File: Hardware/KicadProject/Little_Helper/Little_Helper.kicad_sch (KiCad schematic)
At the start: 36 parts, among them J1 USB_B_Micro_Molex_1050171001_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, J2 Conn_01x02_Pin, Q1 DMG3415U, SW1 SW_Push, SW2 SW_Push, SW3 SW_Push, SW4 SW_Push, SW5 SW_Push, SW6 SW_SPST, SW7 SW_Push, SW8 SW_Push, U1 AP2112K-3.3, U2 ESP32-S3-MINI-1, U3 MCP73831-2-OT

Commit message: Change Boot and Reset BTN
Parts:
- SW7, SW8: footprint Button_Switch_SMD:SW_Push_SPST_NO_Alps_SKRK -> Button_Switch_SMD:SW_SPST_CK_RS282G05A3
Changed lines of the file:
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@@
 			)
 		)
-		(property "Footprint" "Button_Switch_SMD:SW_Push_SPST_NO_Alps_SKRK"
+		(property "Footprint" "Button_Switch_SMD:SW_SPST_CK_RS282G05A3"
 			(at 128.27 105.41 0)
 			(effects
@@
 			)
 		)
-		(property "Footprint" "Button_Switch_SMD:SW_Push_SPST_NO_Alps_SKRK"
+		(property "Footprint" "Button_Switch_SMD:SW_SPST_CK_RS282G05A3"
 			(at 160.02 105.41 0)
 			(effects

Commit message: pcb layout v1.0 done
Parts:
- removed D4: BAS16, ba_sot:sot_23, symbol ba_diode:BAS16
- removed J2: Conn_01x02_Pin, Connector_Hirose:Hirose_DF13-02P-1.25DSA_1x02_P1.25mm_Vertical, symbol Connector:Conn_01x02_Pin
- removed Q1: DMG3415U, Package_TO_SOT_SMD:SOT-23, symbol PCM_Transistor_MOSFET_AKL:DMG3415U
- removed R3: R2012_100K, ba_res:r2012, symbol ba_res2012:R2012_100K
- removed SW6: SW_SPST, Button_Switch_SMD:SW_SPDT_CK_JS102011SAQN, symbol Switch:SW_SPST
- removed SW7, SW8: SW_Push, Button_Switch_SMD:SW_SPST_CK_RS282G05A3, symbol Switch:SW_Push
- added D4: BAS16, ba_sot:sot_23, symbol Diode_JLCPCB:BAS16
- added J2, J3: SOLDER_CON_5x2_TOP, ba_connector:solder_con_5x2_top, symbol ba_connector:SOLDER_CON_5x2_TOP
- added MH1: fit_3_1, ba_mechanic:fit_3_1, symbol ba_mechanic:fit_3_1
- added Q1: DMG3415U, Package_TO_SOT_SMD:SOT-23, symbol PCM_Transistor_MOSFET_JLCPCB:DMG3415U
- added R3: 100k, Resistor_SMD:R_0805_2012Metric, symbol Device:R
- added SW6: SW_On_On, Button_Switch_SMD:SW_SPDT_PCM12, symbol Switch_Wolke:SW_On_On
- added SW7, SW8: SW_Tactile_Small, Button_Switch_SMD_JLCPCB:SW_SPST_TS-1088-AR02016, symbol Switch_Wolke:SW_Tactile_Small
- C1, C3, C4, C5, C6, C8: LCSC (none) -> C1713
- D1: footprint Diode_SMD:D_0805_2012Metric -> Diode_SMD:D_SOD-123
- R1: LCSC C115316 -> C17414
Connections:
- net +3.3V: now also D4.1 (A)
- net +BATT: now also Q1.3 (D), SW6.3 (C)
- net BOOT0: now also SW8.2 (A)
- net GND: now also J2.1 (P1), R3.1, SW7.1 (A), SW8.1 (A)
- net NEOPIX_VDD: now also D4.3 (K), Q1.2 (S)
- net RESET: now also SW7.2 (A)
- net VBUS: now also Q1.1 (G), R3.2
- new net: J3.1 (P1), SW6.2 (B)
- no-connect marks 33 -> 34

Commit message: edit pcb and footprints for pcb rev1.1
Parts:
- D3: footprint LED_SMD:LED_WS2812B_PLCC4_5.0x5.0mm_P3.2mm -> led_smd_JLCPCB:LED_WS2812B_JLCPCB_5.0x5.0mm_P3.2mm
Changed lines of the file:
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@@
 			)
 		)
-		(property "Footprint" "LED_SMD:LED_WS2812B_PLCC4_5.0x5.0mm_P3.2mm"
+		(property "Footprint" "led_smd_JLCPCB:LED_WS2812B_JLCPCB_5.0x5.0mm_P3.2mm"
 			(at 207.01 129.54 0)
 			(effects

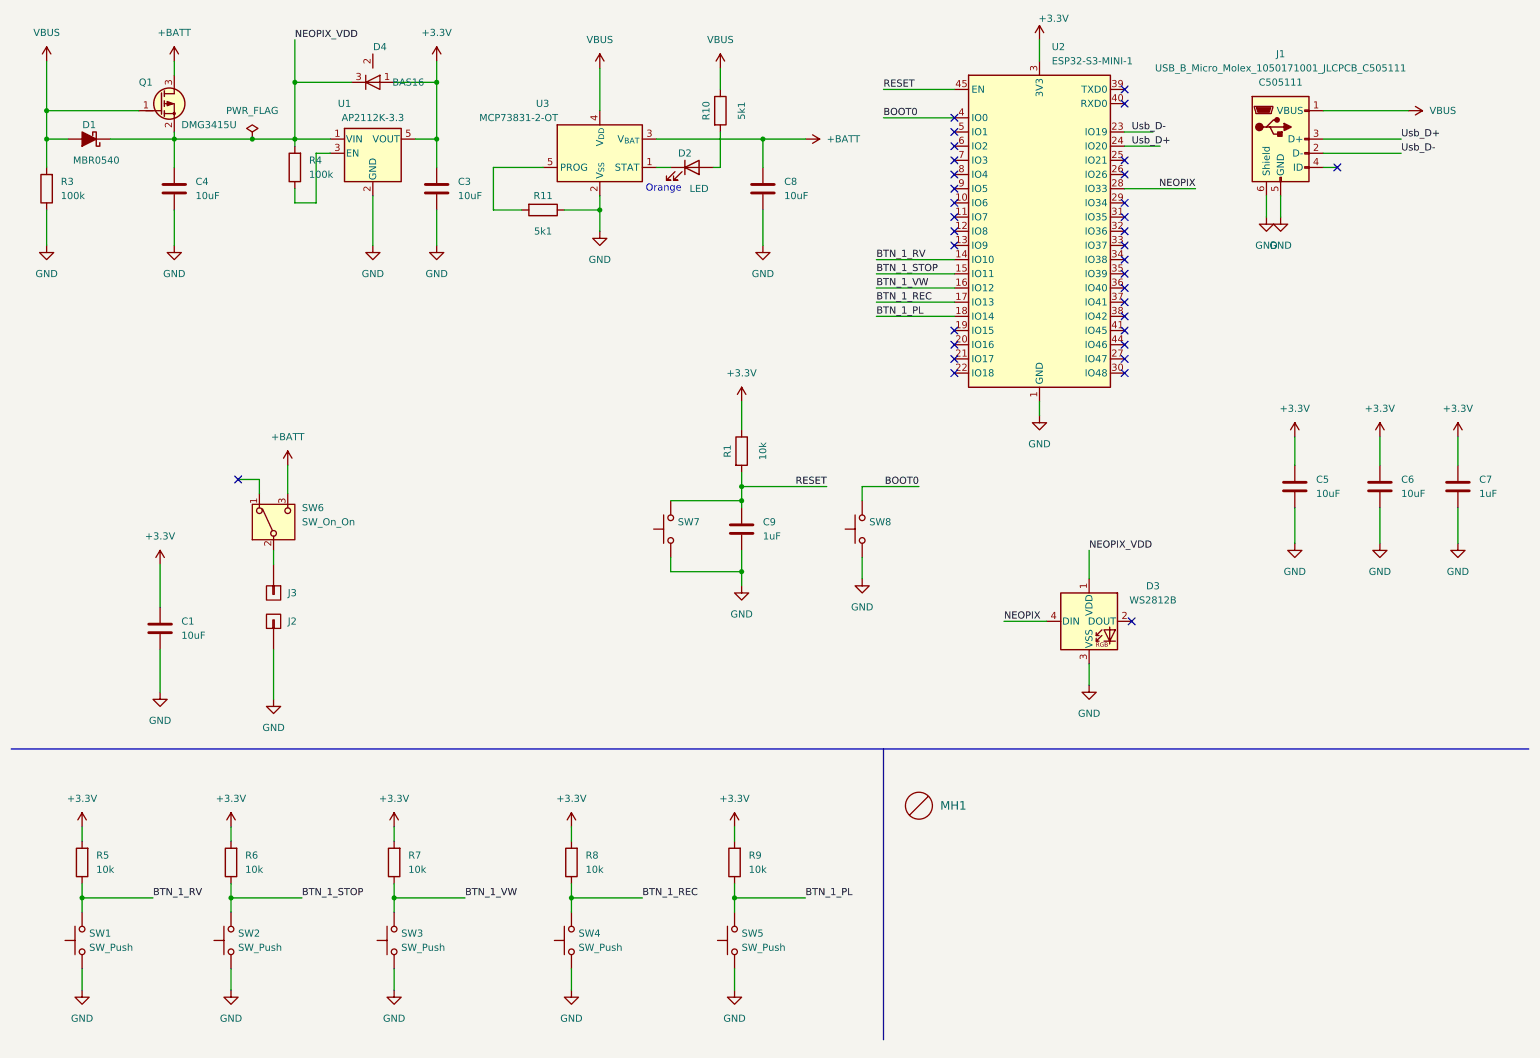
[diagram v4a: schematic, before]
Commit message: pcb v1.1 add second ws2812 led
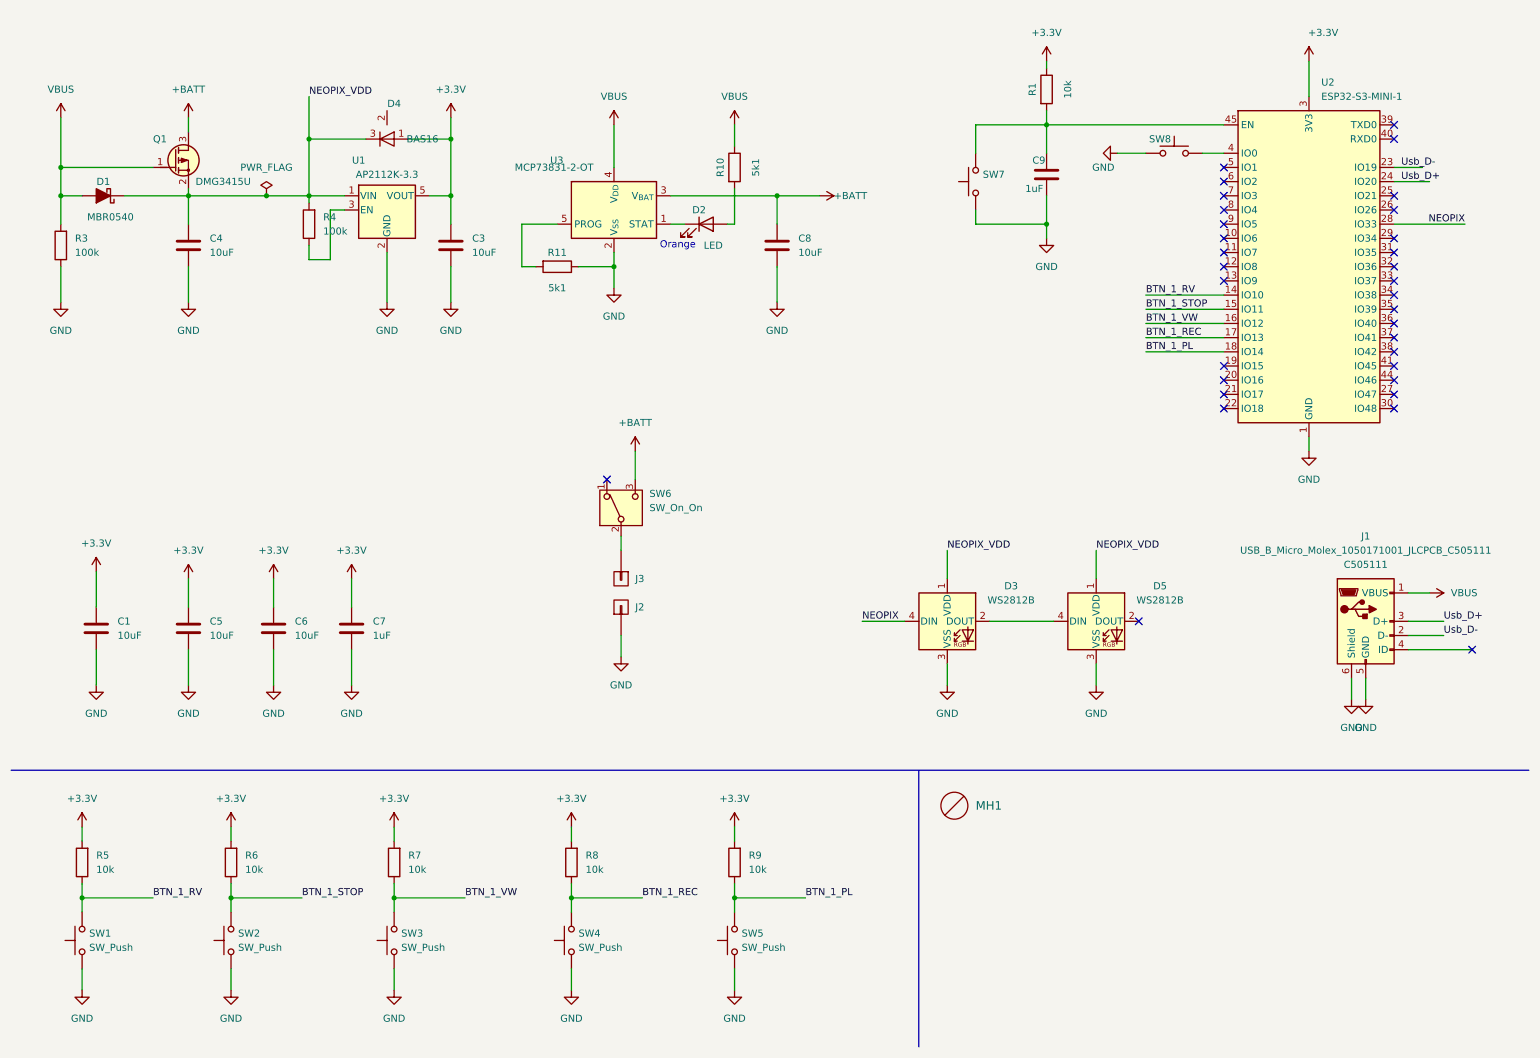
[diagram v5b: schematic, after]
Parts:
- added D5: WS2812B, led_smd_JLCPCB:LED_WS2812B_JLCPCB_5.0x5.0mm_P3.2mm, symbol LED:WS2812B
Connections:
- net GND: now also D5.3 (VSS)
- net NEOPIX_VDD: now also D5.1 (VDD)
- net at D3.2 (DOUT): now also D5.4 (DIN)
- net BOOT0: no longer names the net of SW8.2 (A), U2.4 (IO0)
- net RESET: no longer names the net of C9.1, R1.2, SW7.2 (A), U2.45 (EN)
- no-connect marks 34 -> 33
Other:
- moved on the sheet: C1, C3, C4, C5, C6, C7, C8, C9, D1, D2, D3, D4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

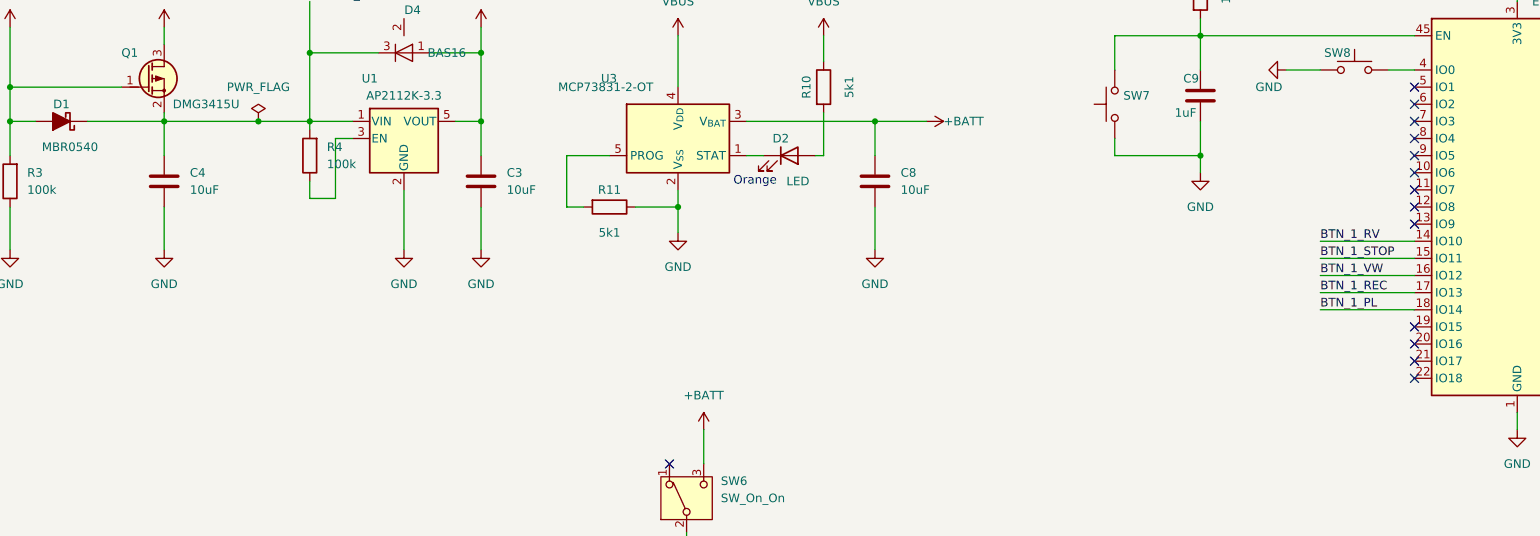
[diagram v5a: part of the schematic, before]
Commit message: add batterie voltage divider. add colorchooser. this commit produce an major bug in button mapping. 2. Map is completly broken.
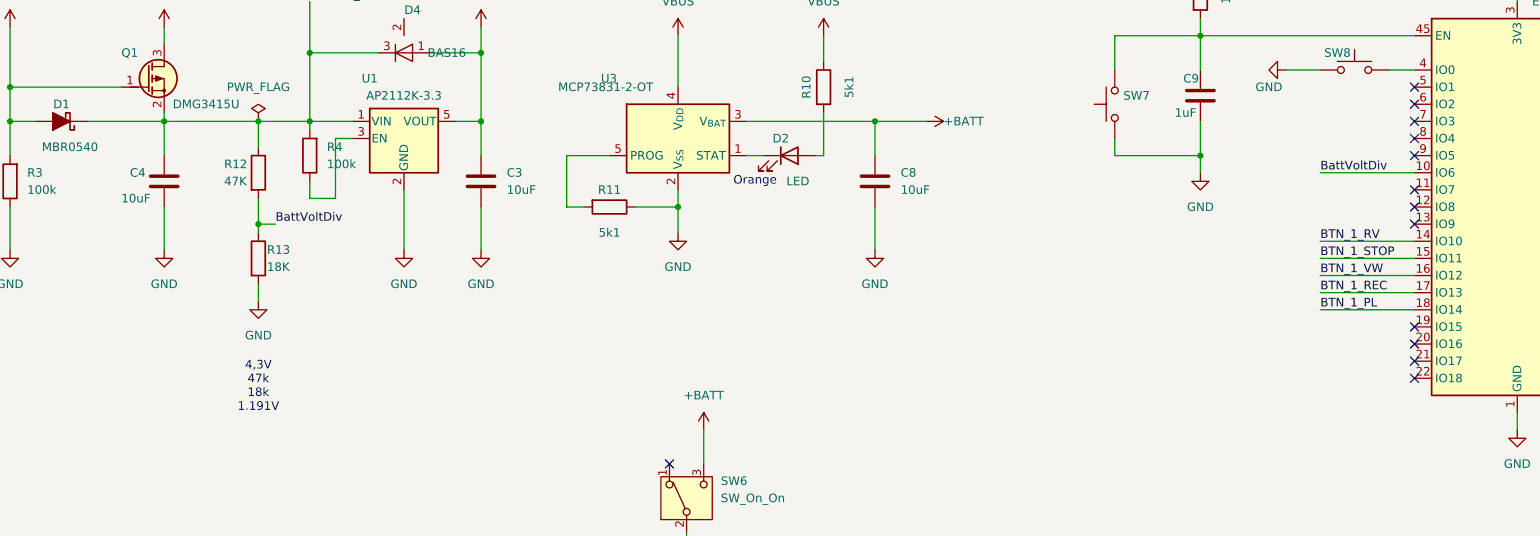
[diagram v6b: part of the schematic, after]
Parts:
- added R12: 47K, ba_res:r2012, symbol Resistor_SMD_0805_JLCPCB:R0805_47K
- added R13: 18K, ba_res:r2012, symbol Resistor_SMD_0805_JLCPCB:R0805_18K
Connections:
- net GND: now also R13.2
- net NEOPIX_VDD: now also R12.1
- net BattVoltDiv: now reaches U2.10 (IO6)
- net BattVoltDiv: now also R12.2, R13.1
- no-connect marks 33 -> 32
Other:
- note added: "4,3V 47k 18k 1.191V"

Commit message: add firmware v7 bin file
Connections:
- net +BATT: now also J3.1 (P1); no longer SW6.3 (C)
- net NEOPIX_VDD: now also SW6.3 (C); no longer C4.1, D1.1 (K), Q1.2 (S)
- net at SW6.2 (B): now also C4.1, D1.1 (K), Q1.2 (S); no longer J3.1 (P1)
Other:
- moved on the sheet: C3, C8, D2, D4, R10, R11, R12, R13, R4, SW6, U1, U3
